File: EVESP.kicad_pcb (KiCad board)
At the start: 2 copper layers, 99.7 x 99.1 mm, 109 parts, among them J1 Screw_Terminal_01x02, J10 Screw_Terminal_01x02, J11 Screw_Terminal_01x02, J12 Screw_Terminal_01x02, J2 Screw_Terminal_01x06, J3 Conn_01x04, J4 Conn_01x16_Male, J5 Conn_01x16_Female, J6 Conn_01x20_Female, J7 Conn_01x20_Male, J8 Screw_Terminal_01x03, J9 Screw_Terminal_01x03, Q1 BC847, Q2 BC847, Q3 BC847, U1 LM7332, U2 MOC3063M, U3 MOC3063M, U4 MOC3063M, U5 LM7332

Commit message: Added gerber and drill files.
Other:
- rule via_min_size: 0.4 -> 0.8

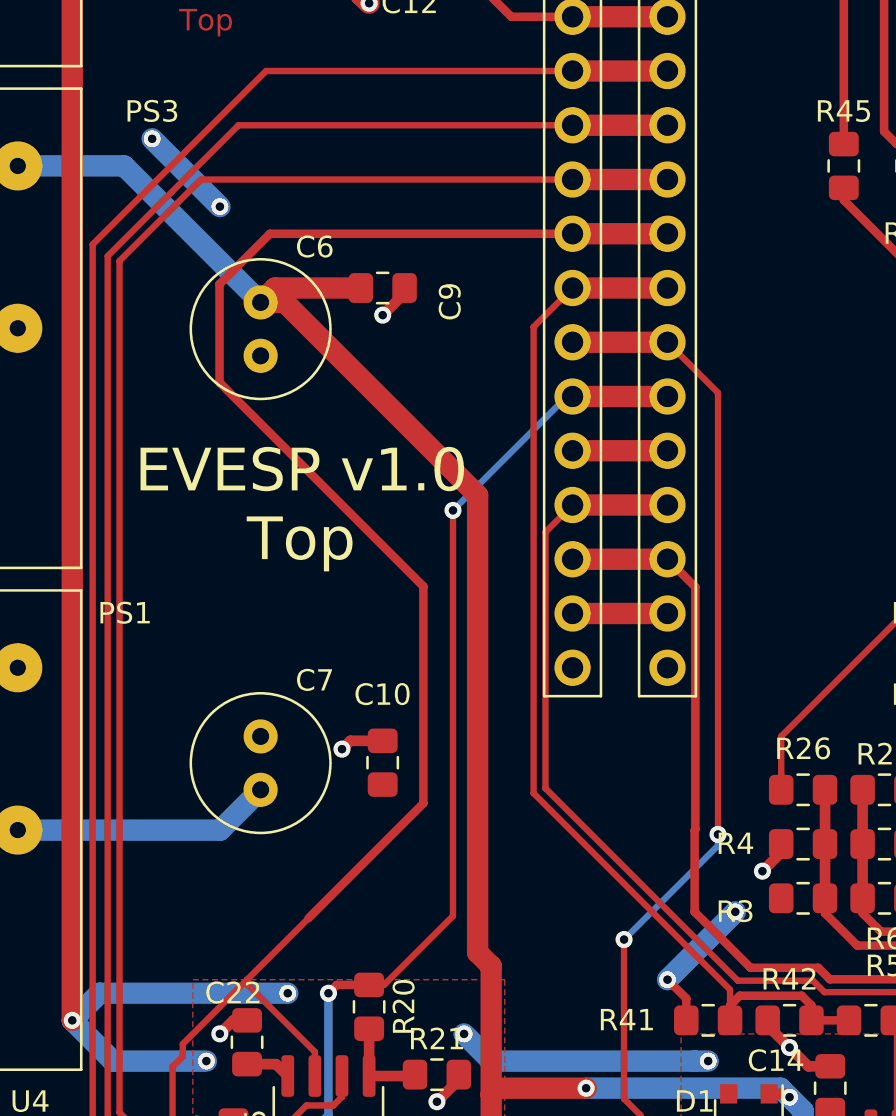
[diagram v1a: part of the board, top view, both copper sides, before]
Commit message: Fixed +-12V drive towards the ESP32 (added resistor and a diode).
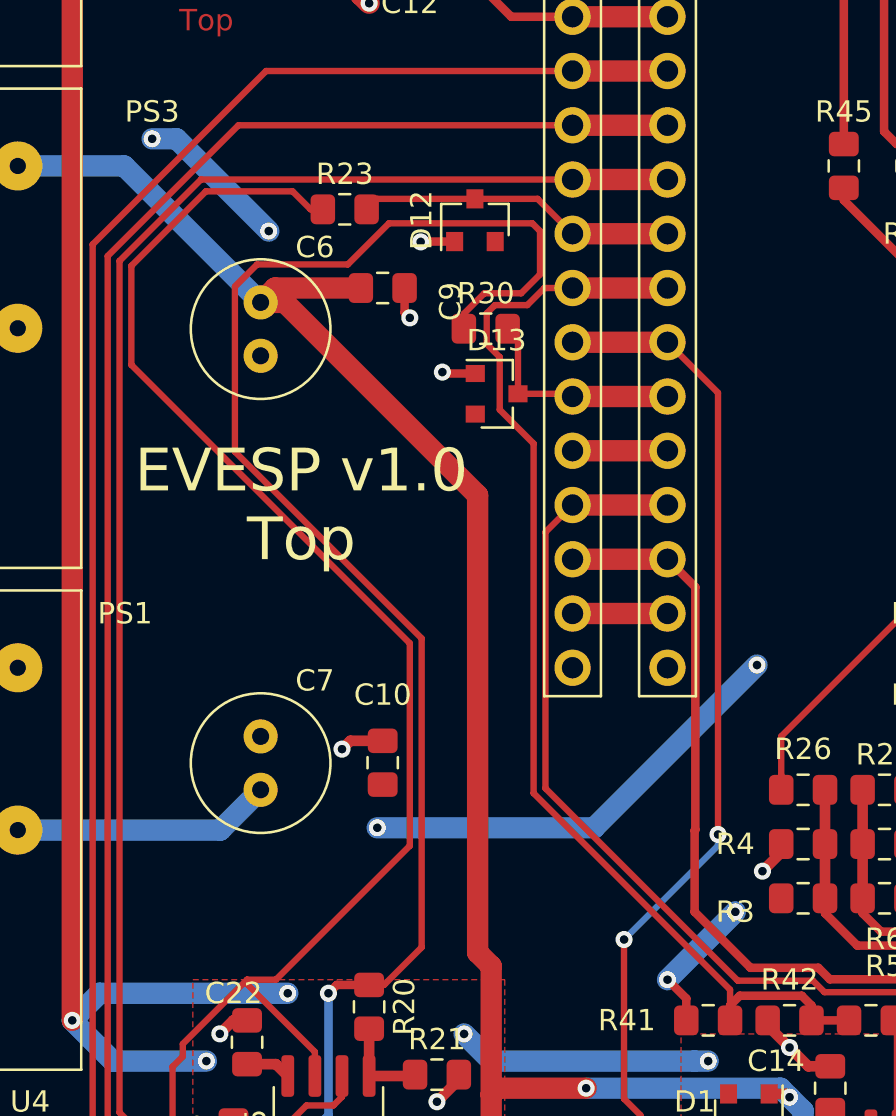
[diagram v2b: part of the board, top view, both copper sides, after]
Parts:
- added D12: BAT54S, Package_TO_SOT_SMD:SOT-23, F.Cu at (107.2, 94.0)
- added D13: BAT54S, Package_TO_SOT_SMD:SOT-23, F.Cu at (108.2, 102.1)
- added R23: 100k, Resistor_SMD:R_0805_2012Metric_Pad1.15x1.40mm_HandSolder, F.Cu at (101.1, 93.5)
- added R30: 100k, Resistor_SMD:R_0805_2012Metric_Pad1.15x1.40mm_HandSolder, F.Cu at (107.7, 99.1)
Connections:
- J4 pad 11: /Charge -> Net-(D13-Pad3)
- J4 pad 8: /SafeToCharge -> Net-(D12-Pad3)
- J5 pad 11: /Charge -> Net-(D13-Pad3)
- J5 pad 8: /SafeToCharge -> Net-(D12-Pad3)
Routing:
- net /Charge: track 51.6 -> 75.6 mm, vias 3 -> 2
- net (no net): track 0.00 -> 20.9 mm, vias 0 -> 1
- net Net-(D12-Pad3): track 0.00 -> 15.0 mm
- net Net-(D13-Pad3): track 0.00 -> 10.3 mm
- net /SafeToCharge: track 90.4 -> 82.1 mm
- net /CP_in: track 50.6 -> 54.1 mm
- net GND: track 78.5 -> 81.8 mm, vias 28 -> 30
- net +3V3: track 39.6 -> 42.3 mm, vias 10 -> 11

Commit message: Gerbers generated: Fixed +-12V drive towards the ESP32 (added resistor and a diode).
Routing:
- net (no net): track 20.9 -> 0.00 mm, vias 1 -> 0
- net GND: track 81.8 -> 102.8 mm, vias 30 -> 32
- net +3V3: vias 11 -> 10
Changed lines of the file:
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@@
   (gr_line (start 144.78 64.135) (end 45.085 64.135) (layer Edge.Cuts) (width 0.1))
   (gr_line (start 144.78 163.195) (end 144.78 64.135) (layer Edge.Cuts) (width 0.1))
-  (via (at 102.616 122.428) (size 0.8) (drill 0.4) (layers F.Cu B.Cu) (net 2))
-  (via (at 120.396 114.808) (size 0.8) (drill 0.4) (layers F.Cu B.Cu) (net 0))
-  (segment (start 112.776 122.428) (end 120.396 114.808) (width 1) (layer B.Cu) (net 0))
-  (segment (start 102.616 122.428) (end 112.776 122.428) (width 1) (layer B.Cu) (net 0))
+  (via (at 102.616 122.428) (size 0.8) (drill 0.4) (layers F.Cu B.Cu) (net 1))
+  (via (at 120.396 114.808) (size 0.8) (drill 0.4) (layers F.Cu B.Cu) (net 1))
+  (segment (start 112.776 122.428) (end 120.396 114.808) (width 1) (layer B.Cu) (net 1))
+  (segment (start 102.616 122.428) (end 112.776 122.428) (width 1) (layer B.Cu) (net 1))
   (segment (start 143.51 120.015) (end 139.065 120.015) (width 1) (layer F.Cu) (net 1) (status 30))
   (via (at 102.235 83.82) (size 0.8) (drill 0.4) (layers F.Cu B.Cu) (net 1))

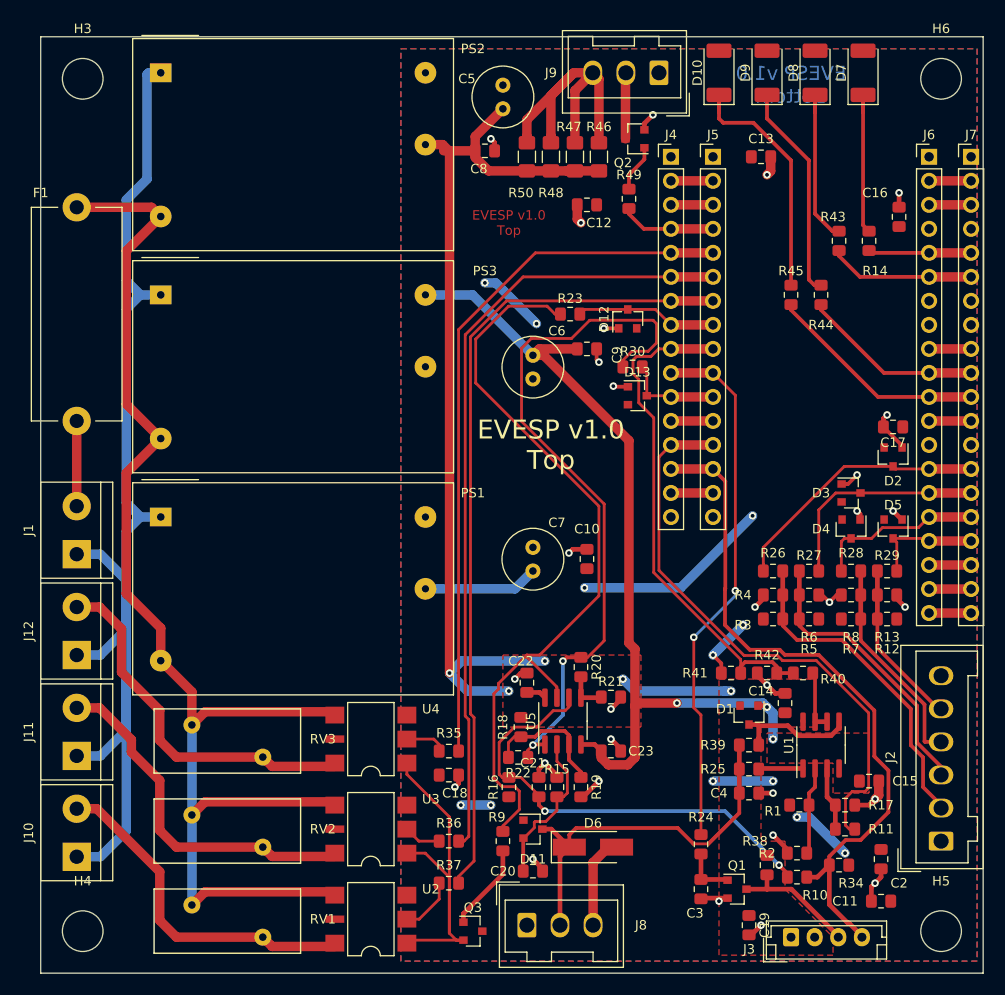
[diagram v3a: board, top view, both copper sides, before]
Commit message: Board cutting fine tuned to leave more clearance on right side connector before edge cut.. Added final production files as zip.
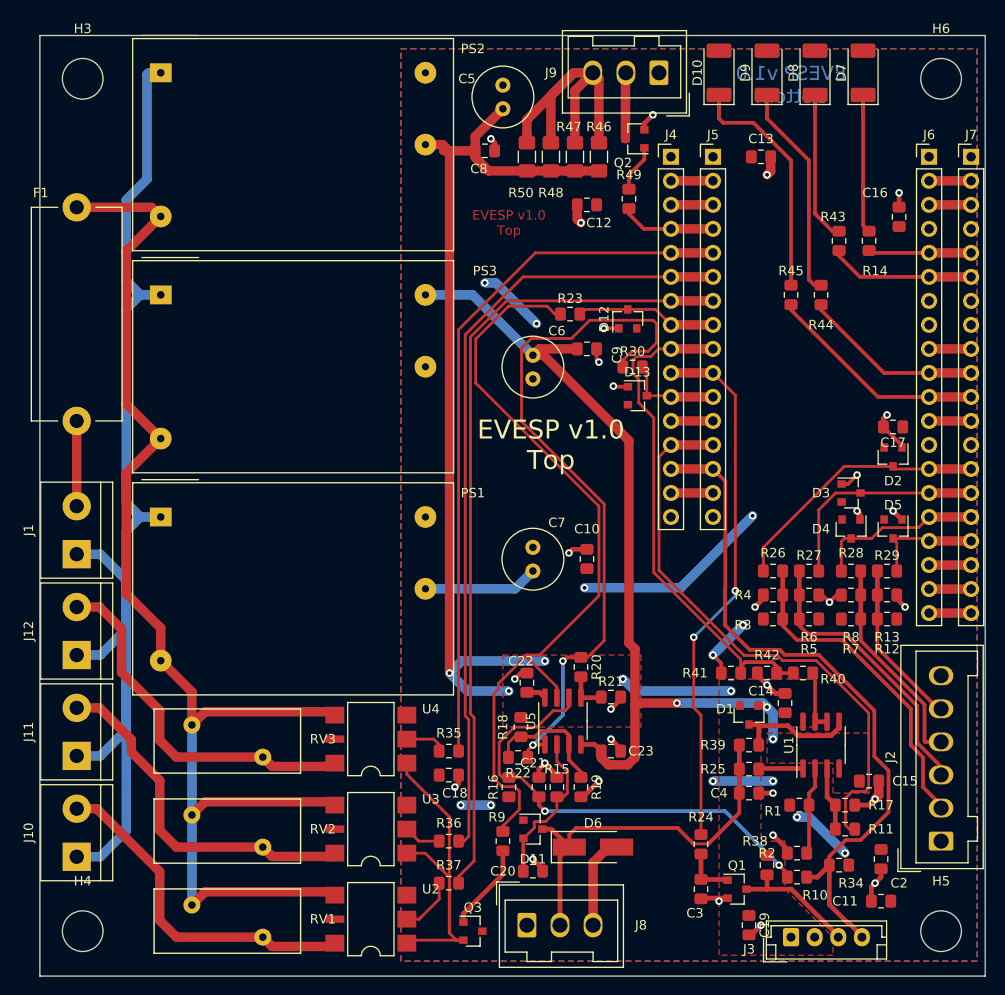
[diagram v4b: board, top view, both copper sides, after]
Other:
- board size 99.7 x 99.1 mm -> 100 x 99.5 mm
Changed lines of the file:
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@@
-(kicad_pcb (version 20171130) (host pcbnew "(5.1.5-0)")
+(kicad_pcb (version 20171130) (host pcbnew "(5.1.5-0-10_14)")
   (general
     (thickness 1.6)
@@
   )
   (setup
-    (last_trace_width 1)
+    (last_trace_width 0.5)
     (user_trace_width 0.3)
     (user_trace_width 0.4)
@@
     (pad_to_mask_clearance 0)
     (aux_axis_origin 138.176 110.617)
+    (grid_origin 45.09 163.19)
     (visible_elements FFFFFF7F)
     (pcbplotparams
@@
     (effects (font (size 2 2) (thickness 0.15)))
   )
-  (gr_line (start 45.085 163.195) (end 144.78 163.195) (layer Edge.Cuts) (width 0.1))
-  (gr_line (start 45.085 64.135) (end 45.085 163.195) (layer Edge.Cuts) (width 0.1))
-  (gr_line (start 144.78 64.135) (end 45.085 64.135) (layer Edge.Cuts) (width 0.1))
-  (gr_line (start 144.78 163.195) (end 144.78 64.135) (layer Edge.Cuts) (width 0.1))
+  (gr_line (start 45 163.5) (end 145 163.5) (layer Edge.Cuts) (width 0.1))
+  (gr_line (start 45 64) (end 45 163.5) (layer Edge.Cuts) (width 0.1))
+  (gr_line (start 145 64) (end 45 64) (layer Edge.Cuts) (width 0.1))
+  (gr_line (start 145 163.5) (end 145 64) (layer Edge.Cuts) (width 0.1))
   (via (at 102.616 122.428) (size 0.8) (drill 0.4) (layers F.Cu B.Cu) (net 1))
   (via (at 120.396 114.808) (size 0.8) (drill 0.4) (layers F.Cu B.Cu) (net 1))
@@
   (segment (start 89.805 156.9) (end 93.98 152.725) (width 0.5) (layer F.Cu) (net 65))
   (segment (start 89.805 157.8) (end 89.805 156.9) (width 0.5) (layer F.Cu) (net 65) (status 10))
-  (segment (start 116.205 102.235) (end 111.76 102.235) (width 1) (layer F.Cu) (net 75) (status 30))
   (segment (start 98.425 139) (end 97.22 139) (width 0.4) (layer F.Cu) (net 66) (status 10))
   (segment (start 97.155 139.065) (end 100.33 135.89) (width 0.4) (layer B.Cu) (net 66))
@@
   (segment (start 93.915 142.485) (end 93.58599 142.15599) (width 0.3) (layer F.Cu) (net 69) (status 10))
   (segment (start 94.615 142.485) (end 93.915 142.485) (width 0.3) (layer F.Cu) (net 69) (status 30))
-  (segment (start 111.76 94.615) (end 116.205 94.615) (width 1) (layer F.Cu) (net 74) (status 30))
   (segment (start 96.52 129.745088) (end 96.52 129.54) (width 0.3) (layer F.Cu) (net 71))
   (segment (start 99.695 134.05) (end 99.695 132.920088) (width 0.3) (layer F.Cu) (net 71) (status 10))
@@
   (segment (start 126.365 144.145) (end 127 143.51) (width 0.4) (layer F.Cu) (net 73))
   (segment (start 126.365 150.25) (end 126.12 150.495) (width 0.4) (layer F.Cu) (net 73) (status 30))
+  (segment (start 111.76 94.615) (end 116.205 94.615) (width 1) (layer F.Cu) (net 74) (status 30))
   (segment (start 110.125 92.98) (end 111.76 94.615) (width 0.3) (layer F.Cu) (net 74))
   (segment (start 107.188 92.98) (end 110.125 92.98) (width 0.3) (layer F.Cu) (net 74))
   (segment (start 102.609 92.98) (end 102.117 93.472) (width 0.3) (layer F.Cu) (net 74))
   (segment (start 107.188 92.98) (end 102.609 92.98) (width 0.3) (layer F.Cu) (net 74))
+  (segment (start 116.205 102.235) (end 111.76 102.235) (width 1) (layer F.Cu) (net 75) (status 30))
   (segment (start 109.229 102.083) (end 109.204 102.108) (width 0.3) (layer F.Cu) (net 75))
   (segment (start 111.633 102.108) (end 111.76 102.235) (width 0.3) (layer F.Cu) (net 75))

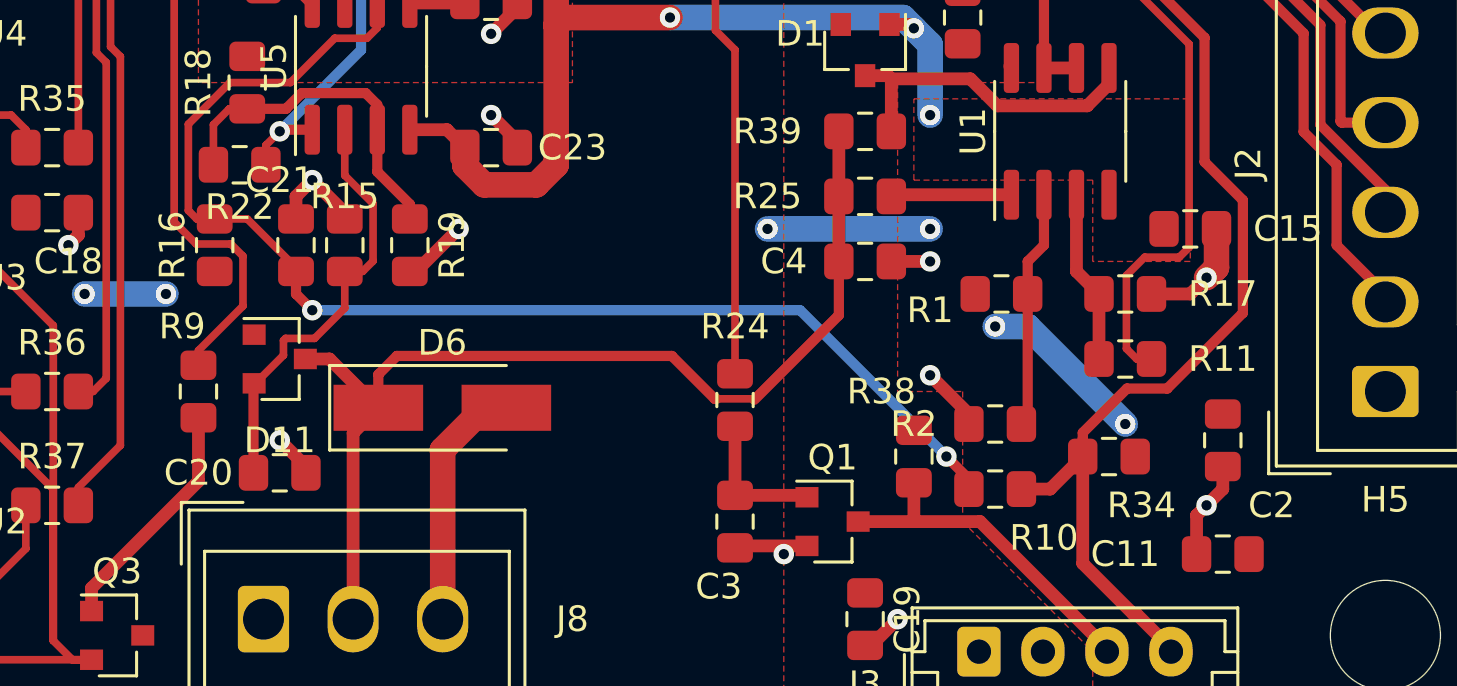
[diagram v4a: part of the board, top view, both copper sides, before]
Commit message: Capacitors now all use capacitor decal (some were using resistor decal).
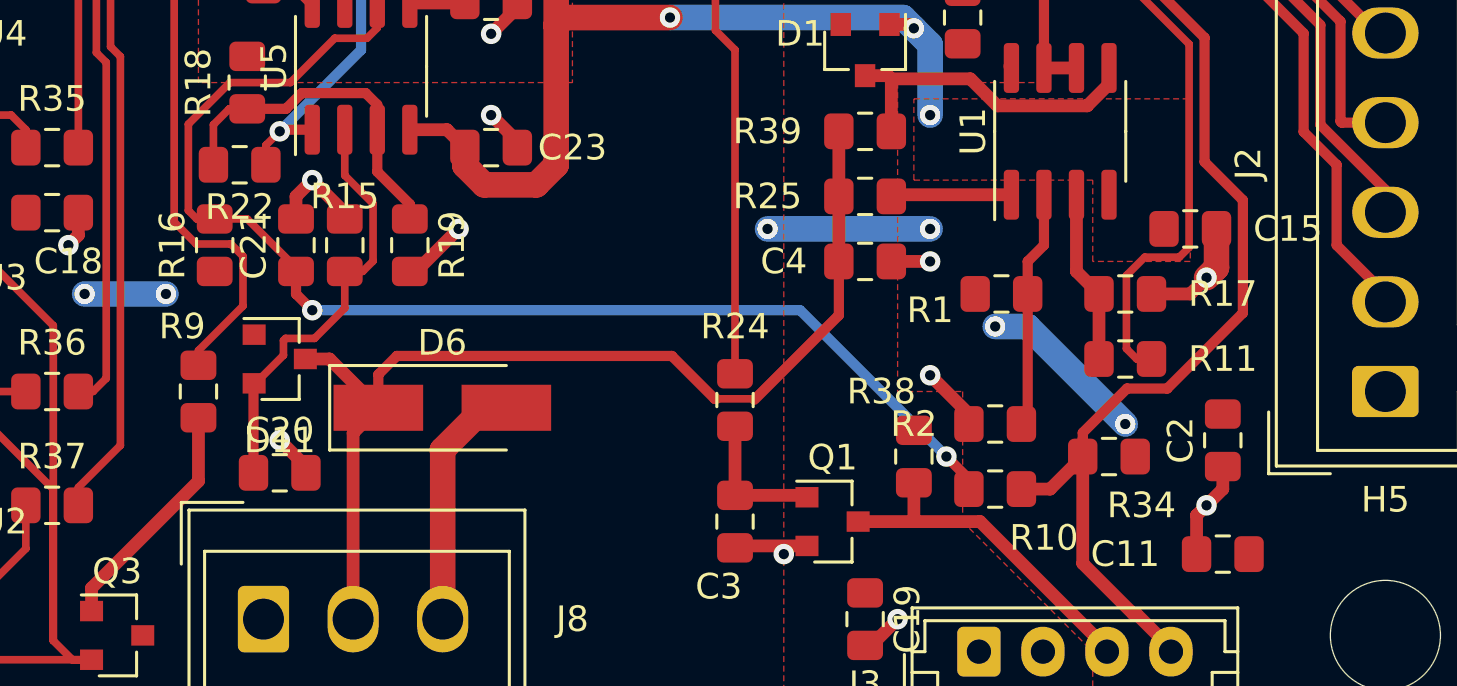
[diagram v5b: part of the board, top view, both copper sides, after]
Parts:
- C19, C2, C20, C21: footprint Resistor_SMD:R_0805_2012Metric_Pad1.15x1.40mm_HandSolder -> Capacitor_SMD:C_0805_2012Metric_Pad1.15x1.40mm_HandSolder
